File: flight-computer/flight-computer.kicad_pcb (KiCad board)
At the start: 2 copper layers, 11 parts, among them J1 Screw_Terminal_01x02, SW1 SW_SPST, U1 MPU6050, U2 BMP180, U3 ESP32_DEVKIT, U4 W25Q64FV_Winbond_Flash_Memory, U5 MPU6050, U6 W25Q64FV_Winbond_Flash_Memory

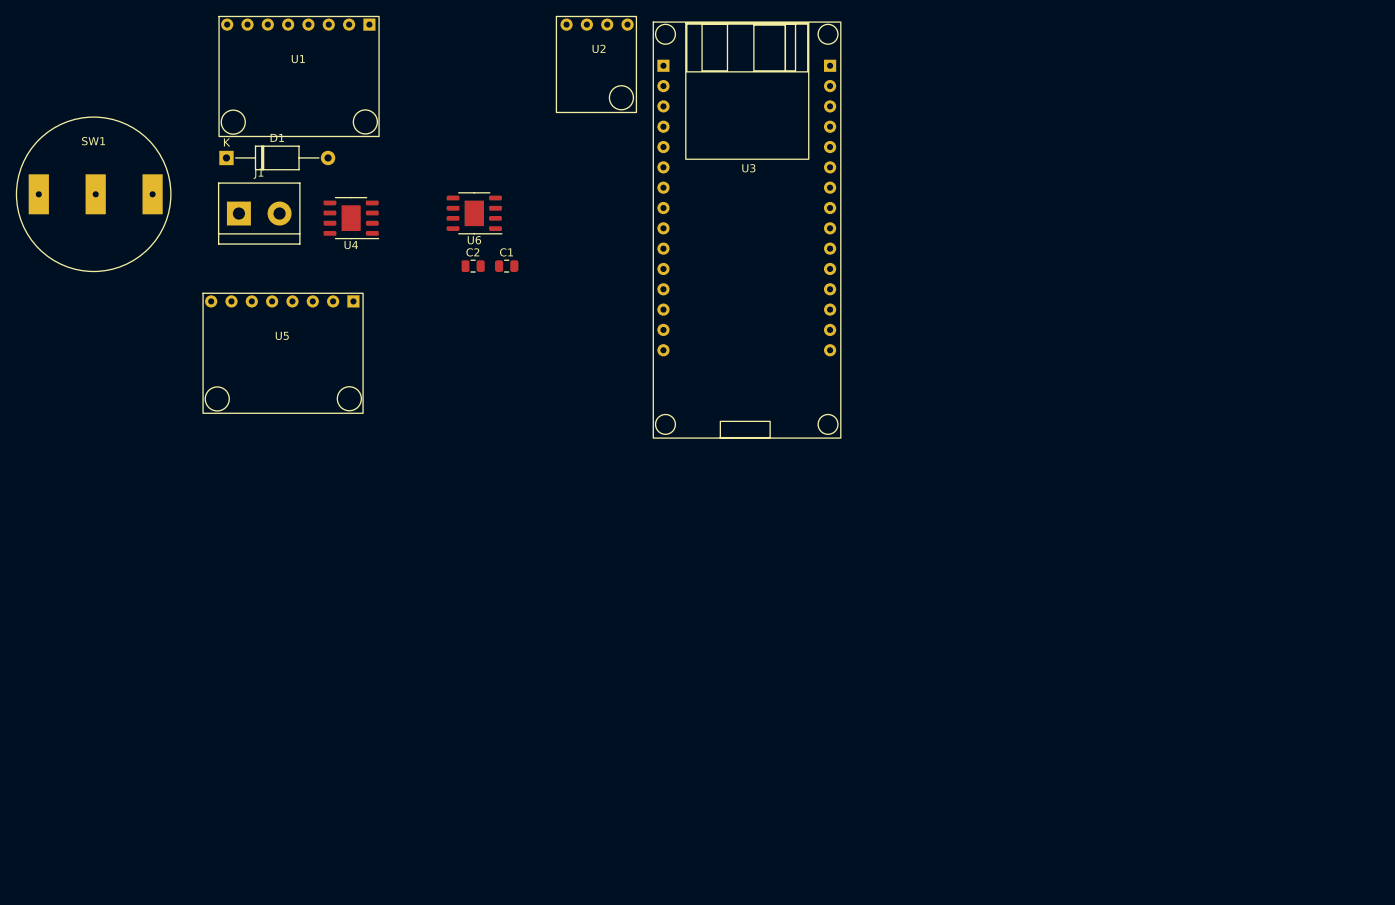
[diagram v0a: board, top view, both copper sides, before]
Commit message: added mounting holes for sensors
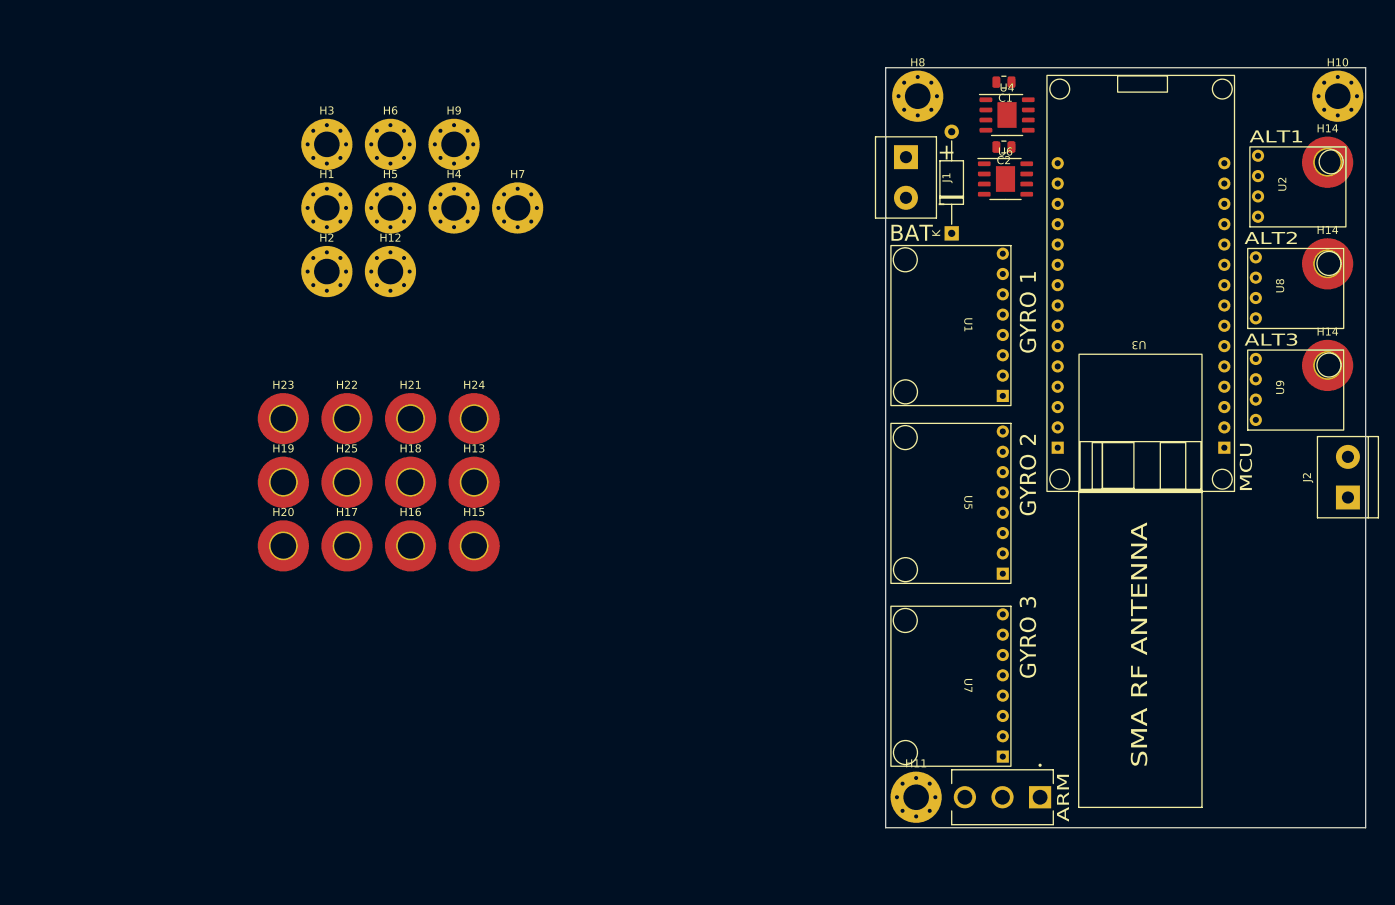
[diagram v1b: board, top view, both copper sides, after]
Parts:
- removed SW1: SW_SPST, custom-footprints:Rocker_Switch_SPST
- added H1: MountingHole_Pad, MountingHole:MountingHole_3.2mm_M3_Pad_Via, F.Cu at (90.2, 49.5)
- added H10: MountingHole_Pad, MountingHole:MountingHole_3.2mm_M3_Pad_Via, F.Cu at (216.5, 35.6)
- added H11: MountingHole_Pad, MountingHole:MountingHole_3.2mm_M3_Pad_Via, F.Cu at (163.8, 123.2)
- added H12: MountingHole_Pad, MountingHole:MountingHole_3.2mm_M3_Pad_Via, F.Cu at (98.1, 57.5)
- added H13: MountingHole_Pad, MountingHole:MountingHole_3.2mm_M3_Pad_TopOnly, F.Cu at (108.6, 83.8)
- added H14: MountingHole_Pad, MountingHole:MountingHole_3.2mm_M3_Pad_TopOnly, F.Cu at (215.3, 69.2)
- added H14: MountingHole_Pad, MountingHole:MountingHole_3.2mm_M3_Pad_TopOnly, F.Cu at (215.3, 43.8)
- added H14: MountingHole_Pad, MountingHole:MountingHole_3.2mm_M3_Pad_TopOnly, F.Cu at (215.3, 56.5)
- added H15: MountingHole_Pad, MountingHole:MountingHole_3.2mm_M3_Pad_TopOnly, F.Cu at (108.6, 91.8)
- added H16: MountingHole_Pad, MountingHole:MountingHole_3.2mm_M3_Pad_TopOnly, F.Cu at (100.6, 91.8)
- added H17: MountingHole_Pad, MountingHole:MountingHole_3.2mm_M3_Pad_TopOnly, F.Cu at (92.7, 91.8)
- added H18: MountingHole_Pad, MountingHole:MountingHole_3.2mm_M3_Pad_TopOnly, F.Cu at (100.6, 83.8)
- added H19: MountingHole_Pad, MountingHole:MountingHole_3.2mm_M3_Pad_TopOnly, F.Cu at (84.7, 83.8)
- added H2: MountingHole_Pad, MountingHole:MountingHole_3.2mm_M3_Pad_Via, F.Cu at (90.2, 57.5)
- added H20: MountingHole_Pad, MountingHole:MountingHole_3.2mm_M3_Pad_TopOnly, F.Cu at (84.7, 91.8)
- added H21: MountingHole_Pad, MountingHole:MountingHole_3.2mm_M3_Pad_TopOnly, F.Cu at (100.6, 75.9)
- added H22: MountingHole_Pad, MountingHole:MountingHole_3.2mm_M3_Pad_TopOnly, F.Cu at (92.7, 75.9)
- added H23: MountingHole_Pad, MountingHole:MountingHole_3.2mm_M3_Pad_TopOnly, F.Cu at (84.7, 75.9)
- added H24: MountingHole_Pad, MountingHole:MountingHole_3.2mm_M3_Pad_TopOnly, F.Cu at (108.6, 75.9)
- added H25: MountingHole_Pad, MountingHole:MountingHole_3.2mm_M3_Pad_TopOnly, F.Cu at (92.7, 83.8)
- added H3: MountingHole_Pad, MountingHole:MountingHole_3.2mm_M3_Pad_Via, F.Cu at (90.2, 41.6)
- added H4: MountingHole_Pad, MountingHole:MountingHole_3.2mm_M3_Pad_Via, F.Cu at (106.1, 49.5)
- added H5: MountingHole_Pad, MountingHole:MountingHole_3.2mm_M3_Pad_Via, F.Cu at (98.1, 49.5)
- added H6: MountingHole_Pad, MountingHole:MountingHole_3.2mm_M3_Pad_Via, F.Cu at (98.1, 41.6)
- added H7: MountingHole_Pad, MountingHole:MountingHole_3.2mm_M3_Pad_Via, F.Cu at (114.0, 49.5)
- added H8: MountingHole_Pad, MountingHole:MountingHole_3.2mm_M3_Pad_Via, F.Cu at (164.0, 35.6)
- added H9: MountingHole_Pad, MountingHole:MountingHole_3.2mm_M3_Pad_Via, F.Cu at (106.1, 41.6)
- added J2: Screw_Terminal_01x02, TerminalBlock:TerminalBlock_bornier-2_P5.08mm, F.Cu at (217.8, 85.7)
- added S1: 100SP1T1B4M2QE, spdt_toggle_switch:SW_100SP1T1B4M2QE, F.Cu at (174.6, 123.2)
- added U7: MPU6050, custom-footprints:MPU6050, F.Cu at (175.7, 99.3)
- added U8: BMP180, custom-footprints:BMP180, F.Cu at (205.3, 64.6)
- added U9: BMP180, custom-footprints:BMP180, F.Cu at (205.3, 77.3)
- moved U1 103.0 mm to (175.7, 54.2), turned to -90 degrees
- moved U5 102.3 mm to (175.7, 76.5), turned to -90 degrees
- moved U3 93.4 mm to (203.6, 85.0), turned to 180 degrees
- moved D1 91.1 mm to (168.3, 52.7), turned to 90 degrees
- moved U2 90.6 mm to (205.6, 51.9), turned to 90 degrees
- moved J1 83.7 mm to (162.6, 43.2), turned to -90 degrees
- moved U4 83.0 mm to (175.2, 37.9), turned to 0 degrees
- moved C2 68.0 mm to (174.8, 41.9), turned to 180 degrees
- moved U6 66.5 mm to (175.0, 45.9), turned to 0 degrees
- moved C1 66.3 mm to (174.8, 33.8), turned to 180 degrees
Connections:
- U3 pad 13: unconnected-(U3-Pad13) -> ACTIVATE_EJECT
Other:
- board outline added: 60 x 95 mm
- board text added: "+"
- board text added: "-"
- board text added: "ALT1"
- board text added: "ALT2"
- board text added: "ALT3"
- board text added: "ARM"
- board text added: "BAT"
- board text added: "GYRO 1"
- board text added: "GYRO 2"
- board text added: "GYRO 3"
- board text added: "MCU"
- board text added: "SMA RF ANTENNA"

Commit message: added NEO6M GPS footprint
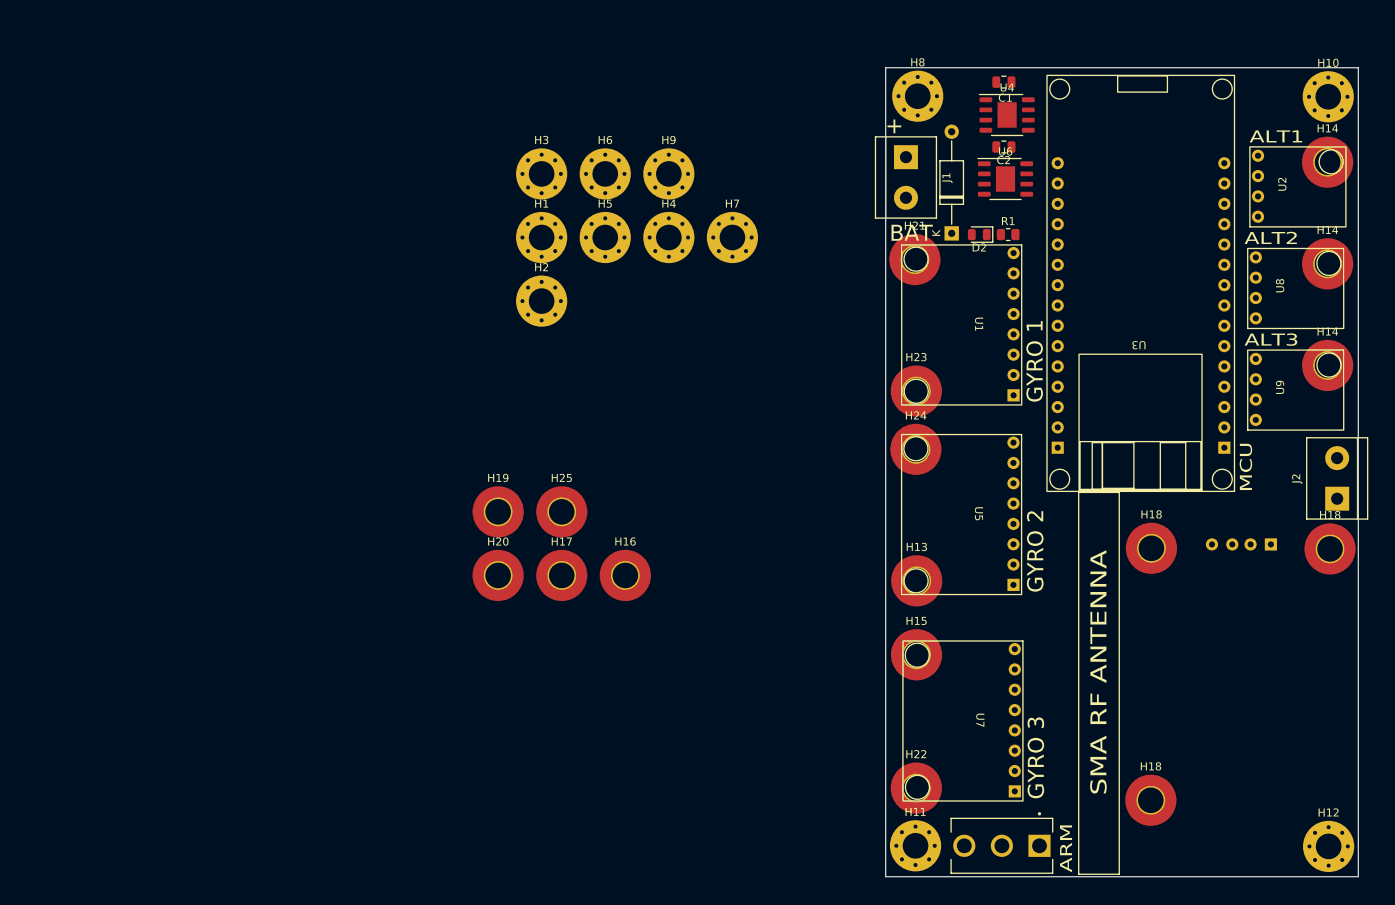
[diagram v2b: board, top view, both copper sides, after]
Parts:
- added D2: LED, LED_SMD:LED_0805_2012Metric, F.Cu at (171.7, 52.9)
- added H18: MountingHole_Pad, MountingHole:MountingHole_3.2mm_M3_Pad_TopOnly, F.Cu at (193.2, 123.6)
- added H18: MountingHole_Pad, MountingHole:MountingHole_3.2mm_M3_Pad_TopOnly, F.Cu at (193.2, 92.1)
- added R1: R, Resistor_SMD:R_0805_2012Metric, F.Cu at (175.3, 52.9)
- added U10: GPS-NEO6M, custom-footprints:GPS-NEO6M, B.Cu at (191.4, 90.3)
- moved H12 137.5 mm to (215.4, 129.3)
- moved H18 115.2 mm to (215.6, 92.2)
- moved H22 84.8 mm to (163.9, 122.0)
- moved H23 79.2 mm to (163.9, 72.4)
- moved H21 66.1 mm to (163.7, 56.0)
- moved H15 56.9 mm to (163.9, 105.4)
- moved H13 56.7 mm to (163.9, 96.1)
- moved H24 55.4 mm to (163.8, 79.7)
- moved H4 27.1 mm to (132.9, 53.2)
- moved H9 27.1 mm to (132.9, 45.3)
- moved H19 27.1 mm to (111.6, 87.5)
- moved H20 27.1 mm to (111.6, 95.5)
- moved H7 27.1 mm to (140.9, 53.2)
- moved H16 27.1 mm to (127.5, 95.5)
- moved H17 27.1 mm to (119.5, 95.5)
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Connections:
- H14 pad 1: (no net) -> GND (x2)
- U3 pad 29: unconnected-(U3-Pad29) -> GPS_TX
- U3 pad 30: unconnected-(U3-Pad30) -> GPS_RX
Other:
- board size 60 x 95 mm -> 59.1 x 101.1 mm
- board text removed: "-"

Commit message: this design is subject to change
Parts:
- added REF**: OSHW-Symbol_6.7x6mm_Copper, Symbol:OSHW-Symbol_6.7x6mm_Copper, F.Cu at (204.2, 123.5)
- moved H17 18.0 mm to (124.5, 78.2)
- moved H25 18.0 mm to (124.5, 70.2)
- moved H16 18.0 mm to (132.4, 78.2)
- moved H19 18.0 mm to (116.5, 70.2)
- moved H20 18.0 mm to (116.5, 78.2)
- moved U2 0.36 mm to (205.2, 51.9)
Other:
- board size 59.1 x 101.1 mm -> 59.1 x 101.4 mm
- board text added: "N3 Flight Computer"

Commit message: removed redundancy
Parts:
- removed U5, U7: MPU6050, custom-footprints:MPU6050

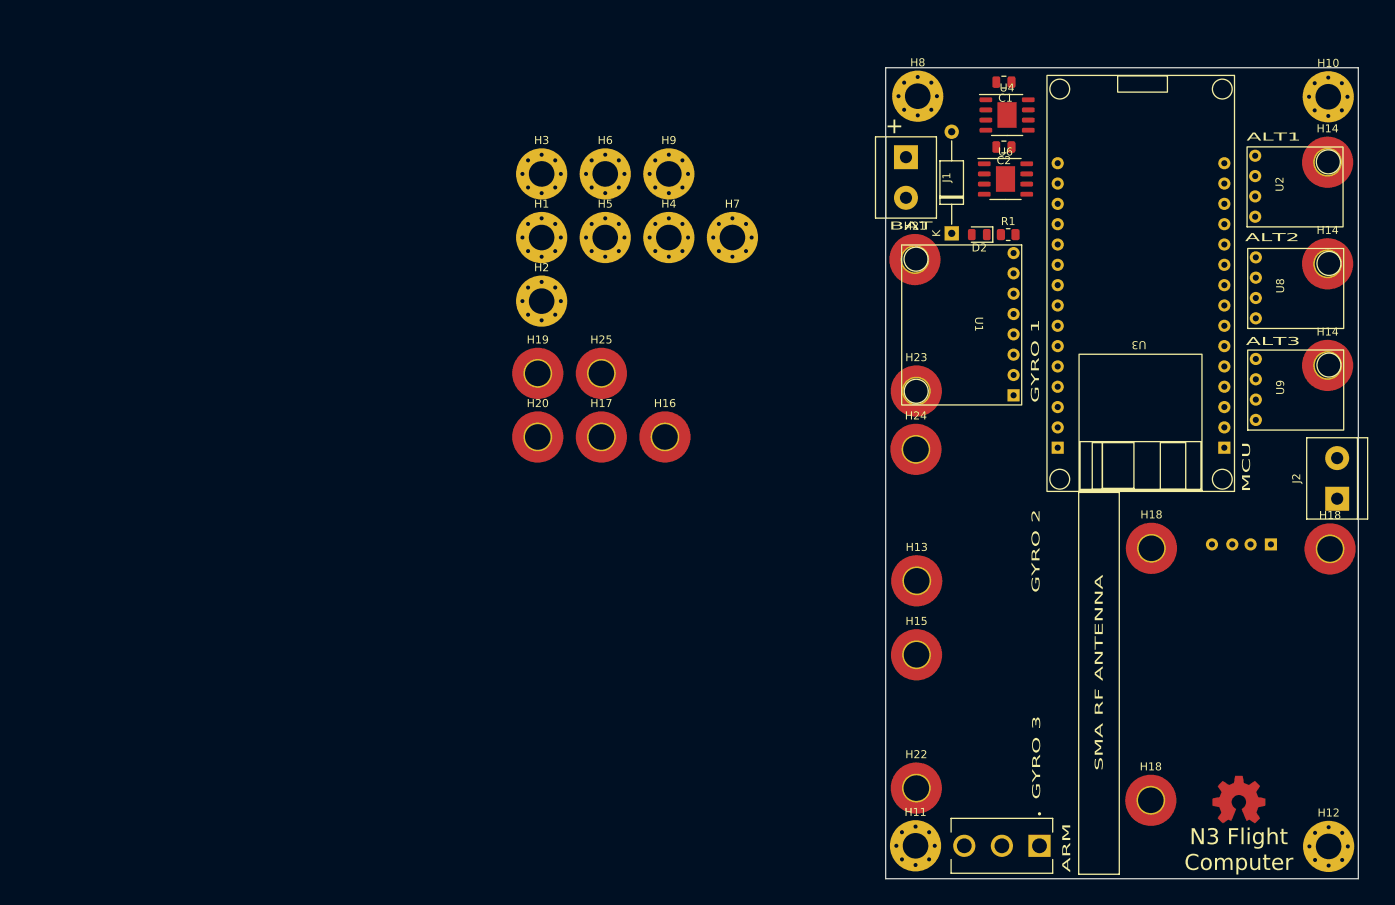
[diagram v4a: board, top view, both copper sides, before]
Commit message: added pcb pdfs
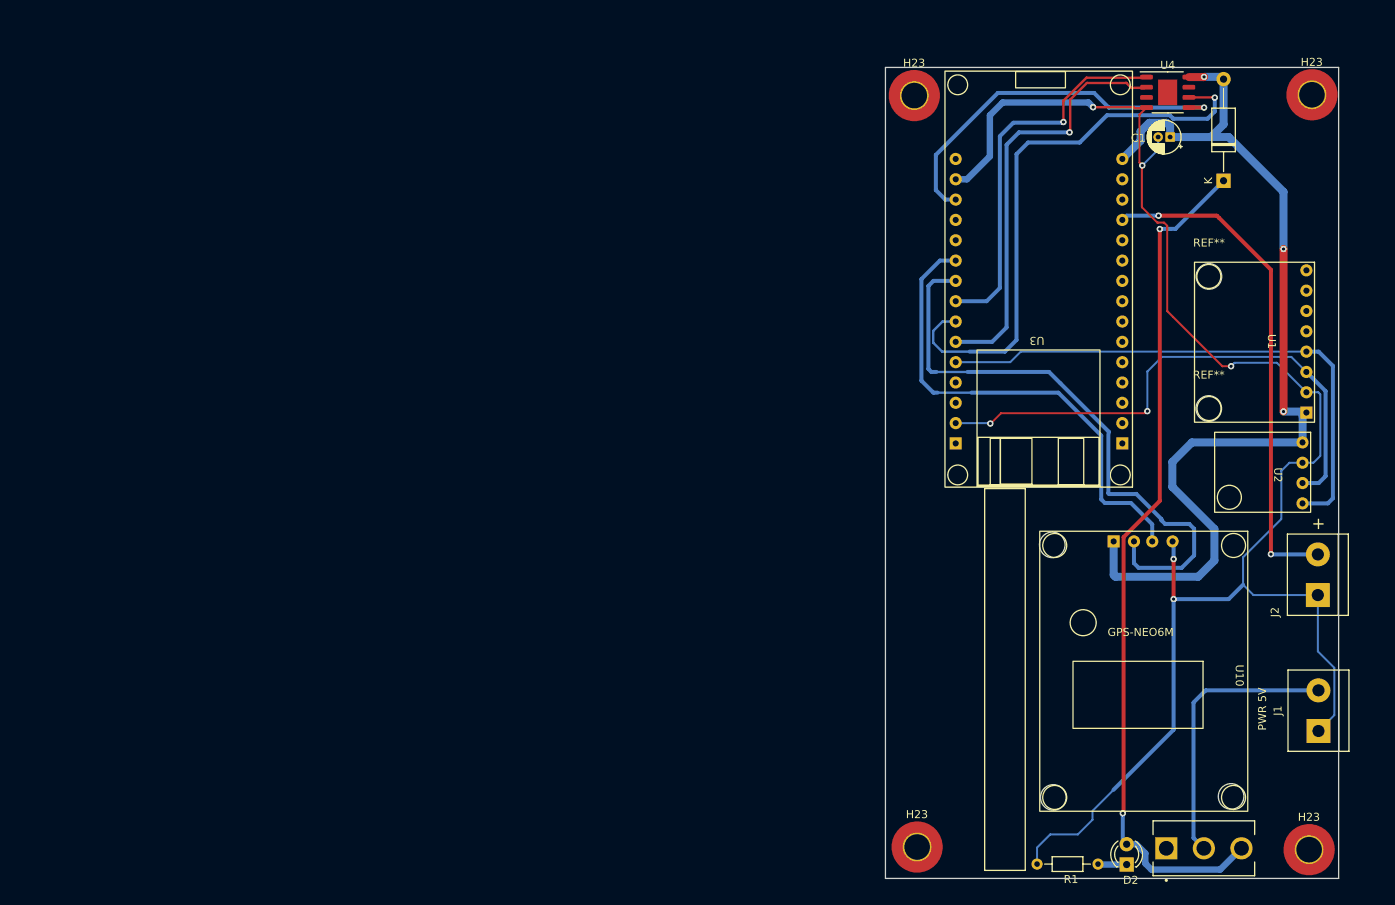
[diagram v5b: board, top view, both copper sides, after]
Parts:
- removed C2: 100nF, Capacitor_SMD:C_0805_2012Metric
- removed H1, H10, H11, H12, H2, H3, H4, H5, H6, H7, H8, H9: MountingHole_Pad, MountingHole:MountingHole_3.2mm_M3_Pad_Via
- removed H13, H14 (x3), H15, H16, H17, H18 (x3), H19, H20, H21, H22, H24, H25: MountingHole_Pad, MountingHole:MountingHole_3.2mm_M3_Pad_TopOnly
- removed the H23 at (163.9, 72.4)
- removed the REF** at (204.2, 123.5)
- removed U6: W25Q64FV_Winbond_Flash_Memory, Package_SO:HTSOP-8-1EP_3.9x4.9mm_P1.27mm_EP2.4x3.2mm
- removed U8, U9: BMP180, custom-footprints:BMP180
- added H23: MountingHole_Pad, MountingHole:MountingHole_3.2mm_M3_Pad_TopOnly, F.Cu at (164.0, 129.4)
- added H23: MountingHole_Pad, MountingHole:MountingHole_3.2mm_M3_Pad_TopOnly, F.Cu at (163.6, 35.5)
- added H23: MountingHole_Pad, MountingHole:MountingHole_3.2mm_M3_Pad_TopOnly, F.Cu at (213.3, 35.4)
- added H23: MountingHole_Pad, MountingHole:MountingHole_3.2mm_M3_Pad_TopOnly, F.Cu at (213.0, 129.7)
- added REF**: MountingHole_3.2mm_M3, MountingHole:MountingHole_3.2mm_M3, F.Cu at (200.4, 74.6)
- added REF**: MountingHole_3.2mm_M3, MountingHole:MountingHole_3.2mm_M3, F.Cu at (200.4, 58.1)
- added REF**: MountingHole_3.2mm_M3, MountingHole:MountingHole_3.2mm_M3, F.Cu at (180.8, 91.6)
- added REF**: MountingHole_3.2mm_M3, MountingHole:MountingHole_3.2mm_M3, F.Cu at (181.0, 123.2)
- added REF**: MountingHole_3.2mm_M3, MountingHole:MountingHole_3.2mm_M3, F.Cu at (203.2, 123.1)
- C1: footprint Capacitor_SMD:C_0805_2012Metric -> Capacitor_THT:CP_Radial_D4.0mm_P1.50mm
- D2: footprint LED_SMD:LED_0805_2012Metric -> LED_THT:LED_D3.0mm
- J1: value Screw_Terminal_01x02 -> PWR 5V
- R1: footprint Resistor_SMD:R_0805_2012Metric -> Resistor_THT:R_Axial_DIN0204_L3.6mm_D1.6mm_P7.62mm_Horizontal
- U10: moved to F.Cu
- moved J1 88.3 mm to (214.1, 114.9), turned to 90 degrees
- moved D2 80.9 mm to (190.1, 131.6), turned to 90 degrees
- moved R1 79.5 mm to (186.6, 131.5), turned to 180 degrees
- moved U1 36.7 mm to (213.6, 56.3)
- moved D1 34.6 mm to (202.3, 46.1)
- moved U2 26.9 mm to (213.1, 77.6), turned to -90 degrees
- moved S1 25.2 mm to (199.8, 129.6), turned to 90 degrees
- moved C1 21.9 mm to (195.6, 40.7)
- moved U4 20.3 mm to (195.3, 35.1)
- moved U10 13.9 mm to (205.3, 89.9)
- moved U3 12.8 mm to (190.9, 84.4)
- moved J2 12.3 mm to (214.0, 97.9)
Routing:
- net GND: track 0.00 -> 203.8 mm, vias 0 -> 5
- net +5V: track 0.00 -> 123.2 mm, vias 0 -> 3
- net Net-(D1-Pad1): track 0.00 -> 107.0 mm, vias 0 -> 2
- net GPS_RX: track 0.00 -> 74.5 mm
- net CLK: track 0.00 -> 71.8 mm, vias 0 -> 1
- net SDA: track 0.00 -> 69.1 mm
- net SCL: track 0.00 -> 68.3 mm, vias 0 -> 2
- net ACTIVATE_EJECT: track 0.00 -> 63.0 mm, vias 0 -> 2
- net GPS_TX: track 0.00 -> 60.6 mm
- net D0: track 0.00 -> 53.0 mm, vias 0 -> 1
- net CS: track 0.00 -> 47.8 mm, vias 0 -> 1
- net DI: track 0.00 -> 46.8 mm, vias 0 -> 1
- net Net-(J1-Pad2): track 0.00 -> 35.0 mm
- net Net-(D2-Pad1): track 0.00 -> 3.60 mm
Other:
- board size 59.1 x 101.4 mm -> 56.6 x 101.4 mm
- board text removed: "ALT1"
- board text removed: "ALT2"
- board text removed: "ALT3"
- board text removed: "ARM"
- board text removed: "BAT"
- board text removed: "GYRO 1"
- board text removed: "GYRO 2"
- board text removed: "GYRO 3"
- board text removed: "MCU"
- board text removed: "N3 Flight Computer"
- board text removed: "SMA RF ANTENNA"
